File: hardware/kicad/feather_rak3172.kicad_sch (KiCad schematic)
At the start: 2 parts, among them J1 Conn_01x16_Female, J2 Conn_01x12_Female

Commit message: initial board design
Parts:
- added C1, C4, C7: 0.1uF, Capacitor_SMD:C_0603_1608Metric, symbol Device:C_Small
- added C10, C12, C8, C9: 10uF, Capacitor_SMD:C_0805_2012Metric, symbol Device:C_Small
- added C11: 100nF, Capacitor_SMD:C_0603_1608Metric_Pad1.08x0.95mm_HandSolder, symbol Device:C_Small
- added C2, C5: ? F, Capacitor_SMD:C_0603_1608Metric, symbol Device:C_Small
- added C3: 10uF, Capacitor_SMD:C_0603_1608Metric, symbol Device:C_Small
- added C6: 10nF, Capacitor_SMD:C_0603_1608Metric, symbol Device:C_Small
- added D1: RED, LED_SMD:LED_0603_1608Metric, symbol Device:LED
- added D2: ORANGE, LED_SMD:LED_0603_1608Metric, symbol Device:LED
- added D3: MBR0540, Diode_SMD:D_SOD-123, symbol Diode:MBR0540
- added H1, H2, H3, H4: MountingHole, MountingHole:MountingHole_2.5mm, symbol Mechanical:MountingHole
- added J3: USB_C_Receptacle_USB2.0, Connector_USB:USB_C_Receptacle_XKB_U262-16XN-4BVC11, symbol Connector:USB_C_Receptacle_USB2.0
- added J4: 915MHz SMA, Teapot:SMA_Amphenol_132289_EdgeMount, symbol Connector:Conn_Coaxial
- added J5: SWD, Connector:Tag-Connect_TC2030-IDC-NL_2x03_P1.27mm_Vertical, symbol Connector_Generic:Conn_01x06
- added J6: JST-2PH, Connector_JST:JST_PH_S2B-PH-SM4-TB_1x02-1MP_P2.00mm_Horizontal, symbol Connector_Generic:Conn_01x02
- added JP1: SolderJumper, Jumper:SolderJumper-2_P1.3mm_Bridged_RoundedPad1.0x1.5mm, symbol Jumper:SolderJumper_2_Bridged
- added L1: ? H, Inductor_SMD:L_0603_1608Metric, symbol Device:L_Small
- added Q1: DMG341, Package_TO_SOT_SMD:SOT-23, symbol Device:Q_PMOS_GSD
- added R1, R2: 1K, Resistor_SMD:R_0603_1608Metric, symbol Device:R_Small
- added R10: 10M, Resistor_SMD:R_0603_1608Metric_Pad0.98x0.95mm_HandSolder, symbol Device:R_Small
- added R3, R4, R5: 5.1K, Resistor_SMD:R_0603_1608Metric, symbol Device:R_Small
- added R6, R7, R8: 10K, Resistor_SMD:R_0603_1608Metric, symbol Device:R_Small
- added R9: 4.7M, Resistor_SMD:R_0603_1608Metric_Pad0.98x0.95mm_HandSolder, symbol Device:R_Small
- added SW1: RESET, Button_Switch_SMD:SW_SPST_B3U-1000P, symbol Switch:SW_Push
- added SW2: BOOT, Button_Switch_SMD:SW_SPST_B3U-1000P, symbol Switch:SW_Push
- added TP1: BOOT, TestPoint:TestPoint_Pad_D1.0mm, symbol Connector:TestPoint
- added U1: RAK3172, Teapot:RAK3172, symbol Teapot:RAK3172
- added U2: CH340E, Package_SO:MSOP-10_3x3mm_P0.5mm, symbol Interface_USB:CH340E
- added U3: MCP73831-2-OT, Package_TO_SOT_SMD:SOT-23-5, symbol Battery_Management:MCP73831-2-OT
- added U4: AP2112K-3.3, Package_TO_SOT_SMD:SOT-23-5, symbol Regulator_Linear:AP2112K-3.3
- J1: value Conn_01x16_Female -> Pin Header; symbol Connector:Conn_01x16_Female -> Connector_Generic:Conn_01x16
- J2: value Conn_01x12_Female -> Pin Header; symbol Connector:Conn_01x12_Female -> Connector_Generic:Conn_01x12
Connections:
- net A0: now also U1.32 (PB3/ADC1)
- net A1: now also U1.31 (PB4/ADC2)
- net A2: now also U1.26 (PB2/ADC3)
- net A3: now also U1.25 (PA10/ADC4)
- net A4: now also JP1.2 (B), U1.3 (PA15/ADC5)
- net EN: now also R8.1, U4.3 (EN)
- net GND: now also C1.1, C10.1, C11.2, C12.1, C2.1, C3.1, C4.1, C5.1, C6.2, C7.2, C8.1, C9.1, D1.2 (A), J3.A1 (GND), J3.A12 (GND), J3.B1 (GND), J3.B12 (GND), J3.S1 (SHIELD), J4.2 (Ext), J5.5 (Pin_5), J6.2 (Pin_2), R10.2, R3.2, R4.2, R5.2, R7.2, SW1.1, SW2.2, U1.11 (GND), U1.17 (GND), U1.18 (GND), U1.23 (GND), U1.28 (GND), U2.3 (GND), U3.2 (VSS), U4.2 (GND); no longer J1.1 (Pin_1)
- net MISO: now also U1.14 (MISO/PA6)
- net MOSI: now also U1.13 (MOSI/PA7)
- net RST: now also C4.2, J5.3 (Pin_3), R1.2, SW1.2, U1.22 (RST)
- net SCK: now also U1.15 (SCK/PA5)
- net SCL: now also U1.9 (SCL/PA12)
- net SDA: now also U1.10 (SDA/PA11)
- net VBUS: now also C6.1, D2.2 (A), D3.2 (A), J3.A4 (VBUS), J3.A9 (VBUS), J3.B4 (VBUS), J3.B9 (VBUS), Q1.1 (G), R7.1, U2.7 (VCC), U3.4 (VDD)
- net 0 RX renamed RXD
- net RXD: now also U1.5 (UART1_RX/PB7)
- net 1 TX renamed TXD
- net TXD: now also U1.4 (UART1_TX/PB6)
- net 10 renamed D10
- net D10: now also U1.6 (PA1)
- net 11 renamed D11
- net D11: now also U1.30 (PB5)
- net 12 renamed D12
- net D12: now also U1.27 (PB12)
- net 13 renamed D13
- net D13: now also R2.1, U1.19 (PA8)
- net 3.3V renamed +3.3V
- net +3.3V: now also C1.2, C10.2, C12.2, C3.2, R1.1, U1.24 (VCC), U4.5 (VOUT)
- net 5 renamed D5
- net D5: now also U1.20 (PA9)
- net 6 renamed D6
- net D6: now also U1.29 (PA0)
- net 9 renamed D9
- net D9: now also U1.16 (SS/PA4)
- net A5 renamed D25
- net D25: now also J5.2 (Pin_2), U1.7 (SWDIO/PA13)
- net AREF: no longer names the net of J1.14 (Pin_14)
- net VBAT renamed +BATT
- net +BATT: now also C8.2, J6.1 (Pin_1), Q1.3 (D), R9.1, U3.3 (VBAT)
- new net: C5.2, J4.1 (In), L1.2
- new net: C9.2, D3.1 (K), Q1.2 (S), R8.2, U4.1 (VIN)
- new net: D2.1 (K), R6.2
- new net: D1.1 (K), R2.2
- new net: C11.1, JP1.1 (A), R10.1, R9.2
- new net: R5.1, U3.5 (PROG)
- new net: J3.A5 (CC1), R3.1
- new net: R6.1, U3.1 (STAT)
- new net: J3.B5 (CC2), R4.1
- new net +3V3: J5.1 (Pin_1)
- new net BOOT0: SW2.1, TP1.1, U1.21 (BOOT0)
- new net CH340_V3: C7.1, U2.10 (V3)
- new net D+: J3.A6 (D+), J3.B6 (D+), U2.1 (UD+)
- new net D-: J3.A7 (D-), J3.B7 (D-), U2.2 (UD-)
- new net D4: J1.1 (Pin_1), J5.4 (Pin_4), U1.8 (SWCLK/PA14)
- new net RF: C2.2, L1.1, U1.12 (RF)
- new net RXD2: U1.1 (UART2_RX/PA3), U2.8 (TXD)
- new net TXD2: U1.2 (UART2_TX/PA2), U2.9 (RXD)
- no-connect marks 0 -> 7
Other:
- note added: "Antenna"
- note added: "Battery Charger"
- note added: "Battery Monitoring"
- note added: "Charge LED"
- note added: "Feather Pin"
- note added: "LED Indicator"
- note added: "Mounting Hole"
- note added: "Power Regulator"
- note added: "R Prog Charge Rate: 10K = 100mA 5K = 200mA 2K = 500mA 1K = 1000mA"
- note added: "RAK3172 System"
- note added: "SWD Debugging Port"
- note added: "SWD used as GPIO"
- note added: "USB-C and UART-Bridge"

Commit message: push initial board layout
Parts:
- removed C12: 10uF, Capacitor_SMD:C_0805_2012Metric, symbol Device:C_Small
- removed C2, C5: ? F, Capacitor_SMD:C_0603_1608Metric, symbol Device:C_Small
- removed L1: ? H, Inductor_SMD:L_0603_1608Metric, symbol Device:L_Small
- added JP2: ENLED, Jumper:SolderJumper-2_P1.3mm_Bridged_RoundedPad1.0x1.5mm, symbol Jumper:SolderJumper_2_Bridged
- J3: footprint Connector_USB:USB_C_Receptacle_XKB_U262-16XN-4BVC11 -> Teapot:USB_C_Receptacle_XKB_U262-16XN-4BVC11
- J4: footprint Teapot:SMA_Amphenol_132289_EdgeMount -> Teapot:SMA_HJTech_023
- J6: footprint Connector_JST:JST_PH_S2B-PH-SM4-TB_1x02-1MP_P2.00mm_Horizontal -> Teapot:JST_PH_S2B-PH-SM4-TB_1x02-1MP_P2.00mm_Horizontal
- JP1: value SolderJumper -> ENBATTMON
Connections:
- net RF: now also J4.1 (In)
- net D10 renamed PA1
- net D11 renamed PB5
- net D12 renamed PB12
- net D13 renamed PA8
- net PA8: now also JP2.2 (B); no longer R2.1
- net D25 renamed PA13
- net D4 renamed PA14
- net D5 renamed PA9
- net D6 renamed PA0
- net D9 renamed PA4
- new net: JP2.1 (A), R2.1
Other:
- moved on the sheet: C10, C9, D3, J4, Q1, R7, R8, U4

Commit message: initial completed wiring
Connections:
- net PA13: now also J2.5 (Pin_5); no longer J1.7 (Pin_7)
- net PA14: now also J2.6 (Pin_6); no longer J1.1 (Pin_1)
- net PB12: now also J1.7 (Pin_7); no longer J2.5 (Pin_5)
- net PB5: now also J1.1 (Pin_1); no longer J2.6 (Pin_6)
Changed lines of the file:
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@@
     (effects (font (size 1.27 1.27)) (justify left bottom))
   )
-  (label "PB5" (at 179.07 113.03 180)
+  (label "PA14" (at 179.07 113.03 180)
     (effects (font (size 1.27 1.27)) (justify right bottom))
   )
@@
     (effects (font (size 1.27 1.27)) (justify left bottom))
   )
-  (label "PA13" (at 138.43 113.03 0)
+  (label "PB12" (at 138.43 113.03 0)
     (effects (font (size 1.27 1.27)) (justify left bottom))
   )
@@
     (effects (font (size 1.27 1.27)) (justify right bottom))
   )
-  (label "PB12" (at 179.07 110.49 180)
+  (label "PA13" (at 179.07 110.49 180)
     (effects (font (size 1.27 1.27)) (justify right bottom))
   )
@@
     (effects (font (size 1.27 1.27)) (justify left bottom))
   )
-  (label "PA14" (at 138.43 128.27 0)
+  (label "PB5" (at 138.43 128.27 0)
     (effects (font (size 1.27 1.27)) (justify left bottom))
   )

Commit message: add revision
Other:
- company: (none) -> Teapot Laboratories
- title: (none) -> Feather RAK3172
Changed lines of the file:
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@@
 (kicad_sch (version 20211123) (generator eeschema)
   (paper "A4")
+  (title_block
+    (title "Feather RAK3172")
+    (date "2022-12-31")
+    (rev "1.0")
+    (company "Teapot Laboratories")
+  )
   (junction (at 231.14 121.92) (diameter 0) (color 0 0 0 0)
   )

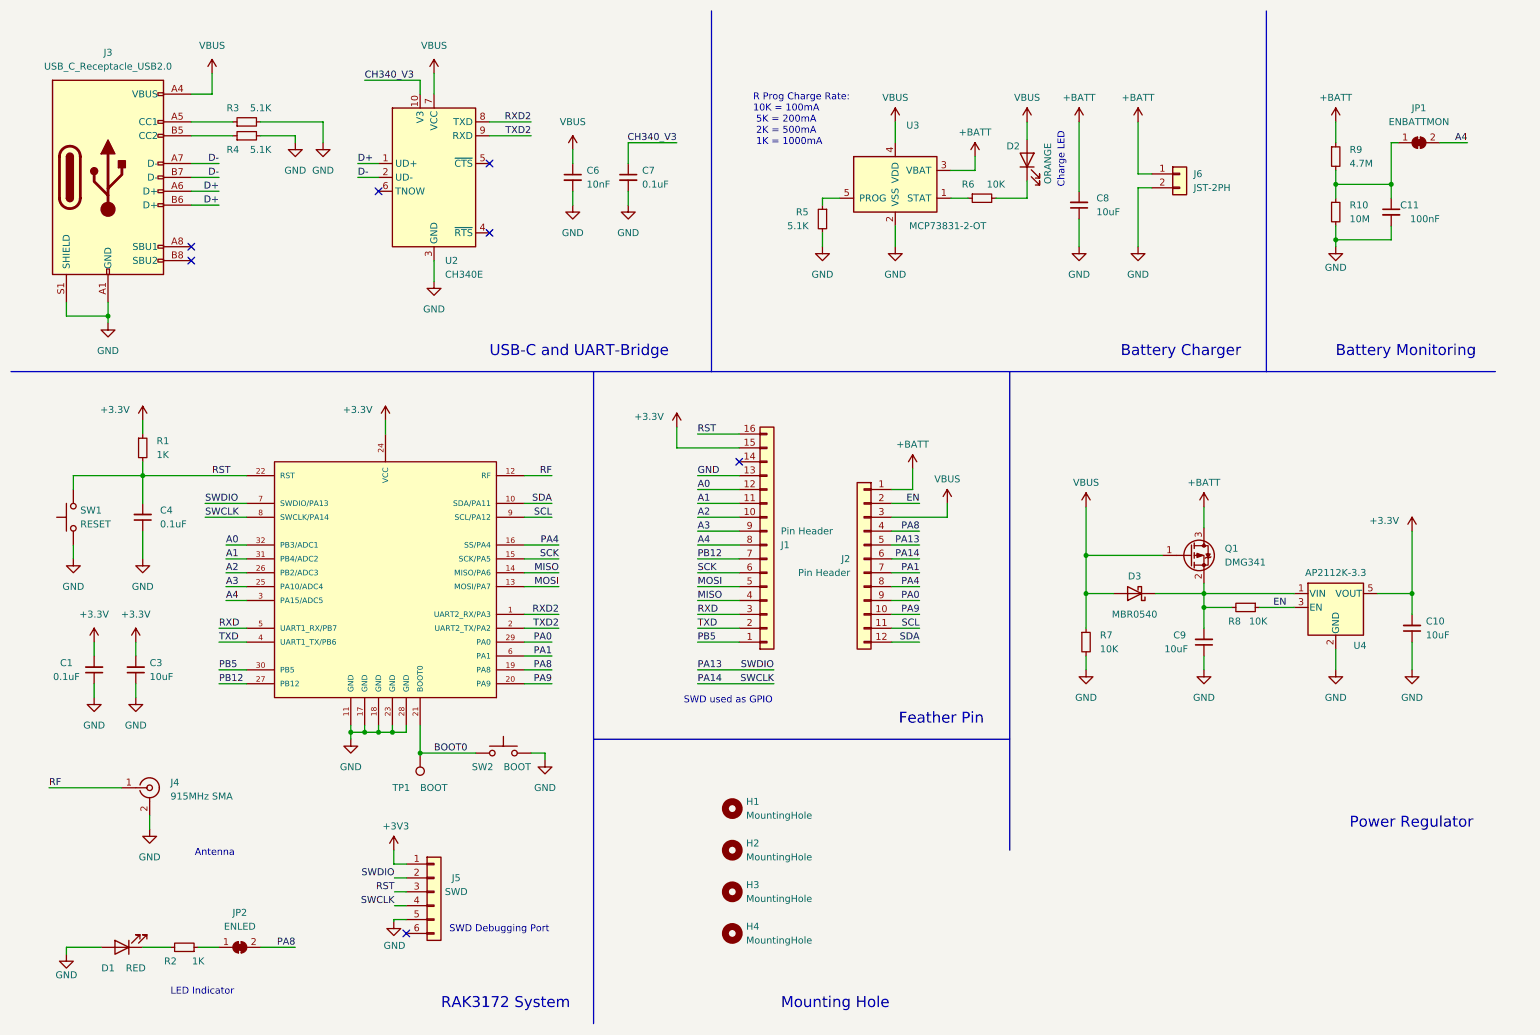
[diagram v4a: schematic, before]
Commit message: add impedance matching circuit and jumper to disable ch340, voltage divider
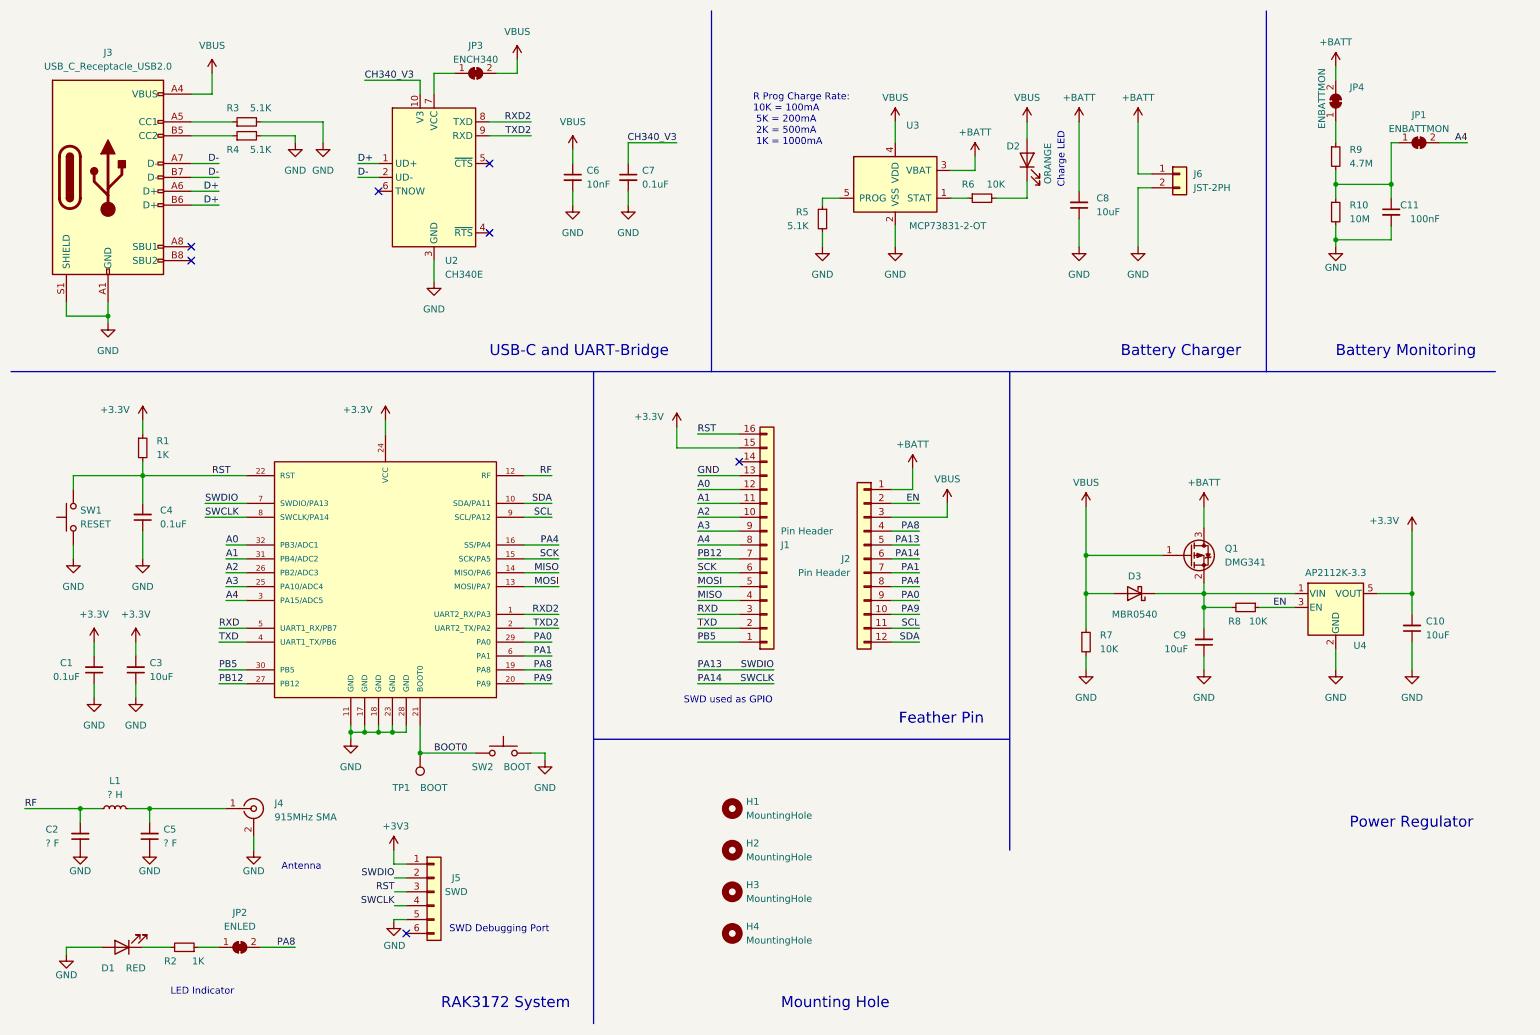
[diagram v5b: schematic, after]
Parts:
- added C2, C5: ? F, Capacitor_SMD:C_0402_1005Metric, symbol Device:C_Small
- added JP3: ENCH340, Jumper:SolderJumper-2_P1.3mm_Bridged_RoundedPad1.0x1.5mm, symbol Jumper:SolderJumper_2_Bridged
- added JP4: ENBATTMON, Jumper:SolderJumper-2_P1.3mm_Bridged_RoundedPad1.0x1.5mm, symbol Jumper:SolderJumper_2_Bridged
- added L1: ? H, Inductor_SMD:L_0402_1005Metric, symbol Device:L_Small
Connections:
- net +BATT: now also JP4.2 (B); no longer R9.1
- net GND: now also C2.1, C5.1
- net RF: now also C2.2, L1.1; no longer J4.1 (In)
- net VBUS: now also JP3.2 (B); no longer U2.7 (VCC)
- new net: C5.2, J4.1 (In), L1.2
- new net: JP3.1 (A), U2.7 (VCC)
- new net: JP4.1 (A), R9.1
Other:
- moved on the sheet: J4

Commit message: breakout D+ and D-, fix incorrect ch340e power wiring, add minor comments
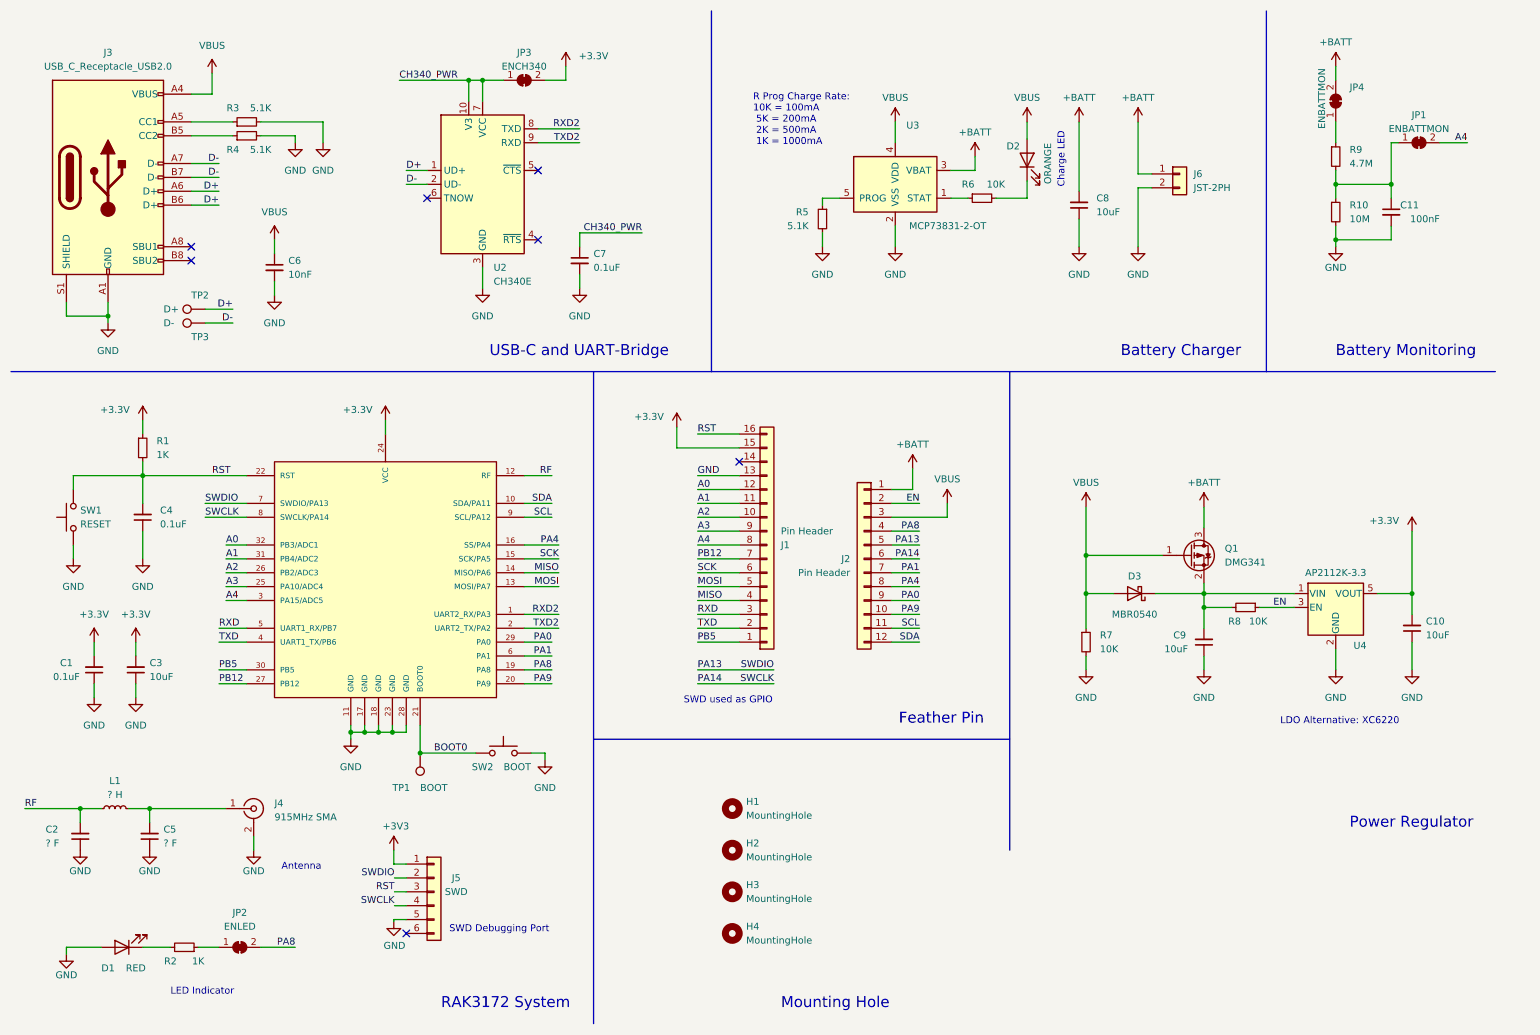
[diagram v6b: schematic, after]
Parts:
- added TP2: D+, TestPoint:TestPoint_Pad_D1.0mm, symbol Connector:TestPoint
- added TP3: D-, TestPoint:TestPoint_Pad_D1.0mm, symbol Connector:TestPoint
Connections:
- net CH340_V3 is gone; now on net CH340_PWR: C7.1, U2.10 (V3)
- net +3.3V: now also JP3.2 (B)
- net D+: now also TP2.1
- net D-: now also TP3.1
- net VBUS: no longer JP3.2 (B)
- net CH340_PWR: now reaches JP3.1 (A), U2.7 (VCC)
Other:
- note added: "LDO Alternative: XC6220"
- moved on the sheet: C6, C7, JP3, U2

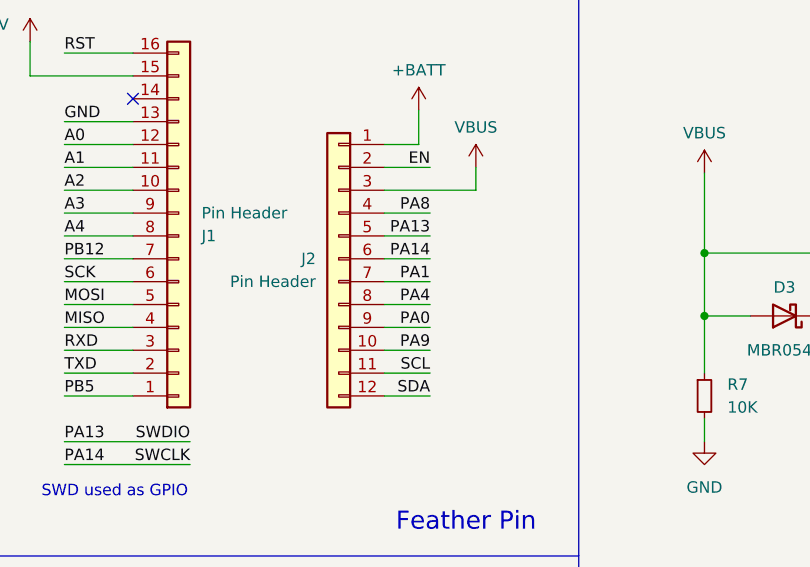
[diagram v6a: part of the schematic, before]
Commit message: remove unnecessary ground pour
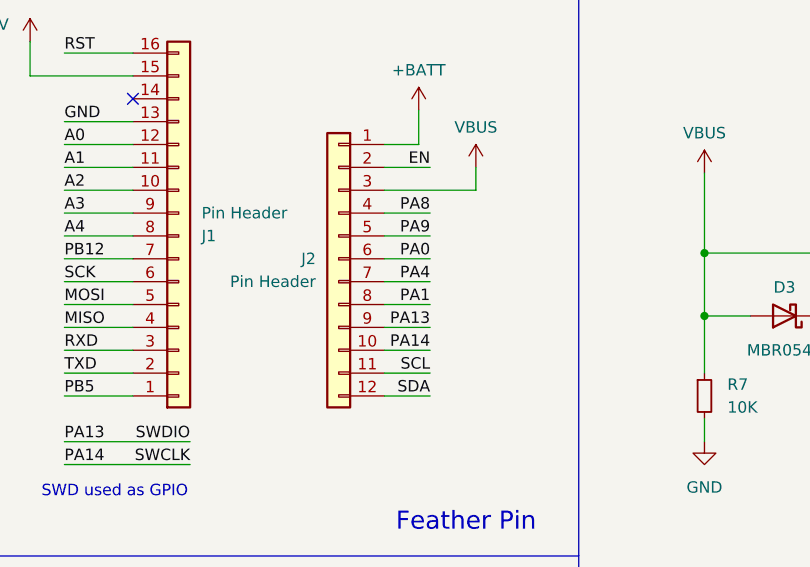
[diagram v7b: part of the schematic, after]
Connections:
- net PA0: now also J2.6 (Pin_6); no longer J2.9 (Pin_9)
- net PA1: now also J2.8 (Pin_8); no longer J2.7 (Pin_7)
- net PA13: now also J2.9 (Pin_9); no longer J2.5 (Pin_5)
- net PA14: now also J2.10 (Pin_10); no longer J2.6 (Pin_6)
- net PA4: now also J2.7 (Pin_7); no longer J2.8 (Pin_8)
- net PA9: now also J2.5 (Pin_5); no longer J2.10 (Pin_10)
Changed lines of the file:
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@@
     (effects (font (size 1.27 1.27)) (justify left bottom))
   )
-  (label "PA14" (at 179.07 113.03 180)
+  (label "PA14" (at 179.07 123.19 180)
     (effects (font (size 1.27 1.27)) (justify right bottom))
   )
@@
     (effects (font (size 1.27 1.27)) (justify right bottom))
   )
-  (label "PA1" (at 179.07 115.57 180)
+  (label "PA1" (at 179.07 118.11 180)
     (effects (font (size 1.27 1.27)) (justify right bottom))
   )
-  (label "PA13" (at 179.07 110.49 180)
+  (label "PA13" (at 179.07 120.65 180)
     (effects (font (size 1.27 1.27)) (justify right bottom))
   )
@@
     (effects (font (size 1.27 1.27)) (justify right bottom))
   )
-  (label "PA9" (at 179.07 123.19 180)
+  (label "PA9" (at 179.07 110.49 180)
     (effects (font (size 1.27 1.27)) (justify right bottom))
   )
@@
     (effects (font (size 1.27 1.27)) (justify left bottom))
   )
-  (label "PA0" (at 179.07 120.65 180)
+  (label "PA0" (at 179.07 113.03 180)
     (effects (font (size 1.27 1.27)) (justify right bottom))
   )
@@
     (effects (font (size 1.27 1.27)) (justify left bottom))
   )
-  (label "PA4" (at 179.07 118.11 180)
+  (label "PA4" (at 179.07 115.57 180)
     (effects (font (size 1.27 1.27)) (justify right bottom))
   )
